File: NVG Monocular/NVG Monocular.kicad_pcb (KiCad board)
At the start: 2 copper layers, 26 parts, among them J1 USB4105-GF-A, J2 breakout to header pin, J3 I2C Breakout, J4 breakout to batt, U1 MP2696AGQ-0000-P

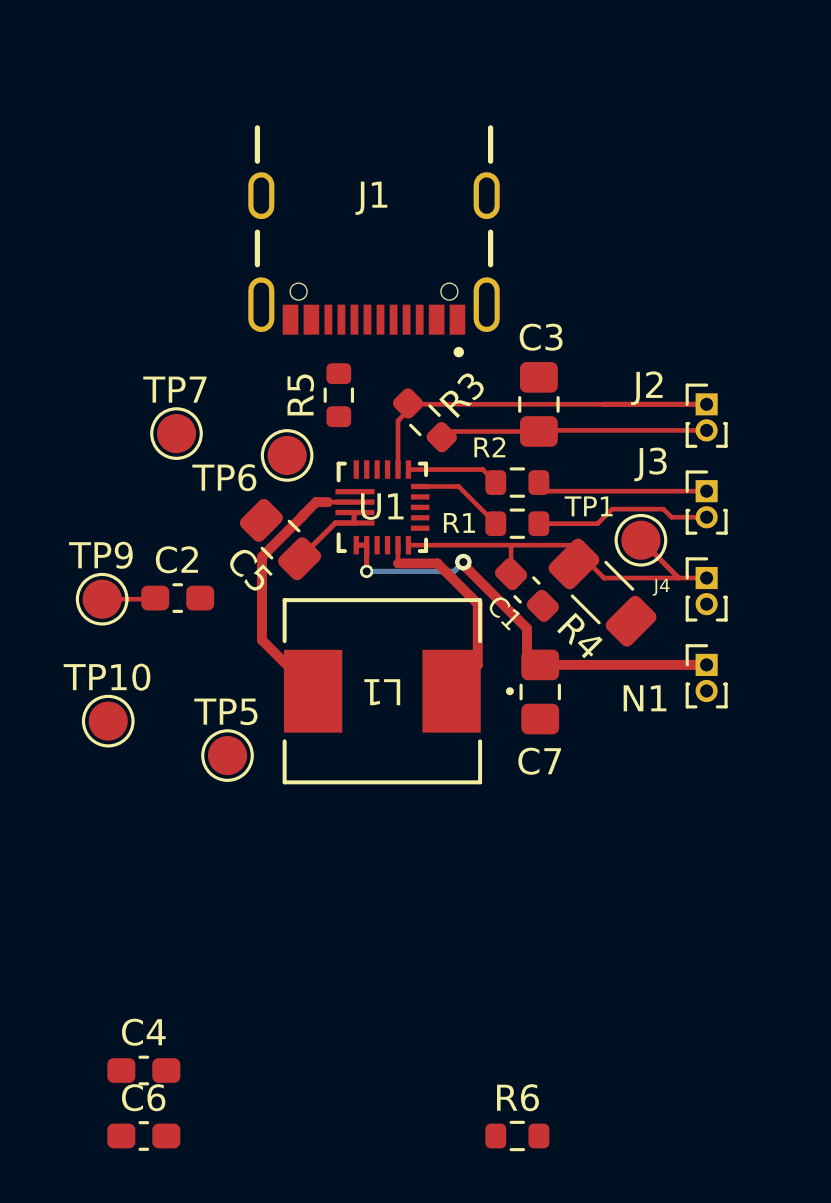
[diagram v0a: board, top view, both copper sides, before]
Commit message: V1 breakout completed and ordered
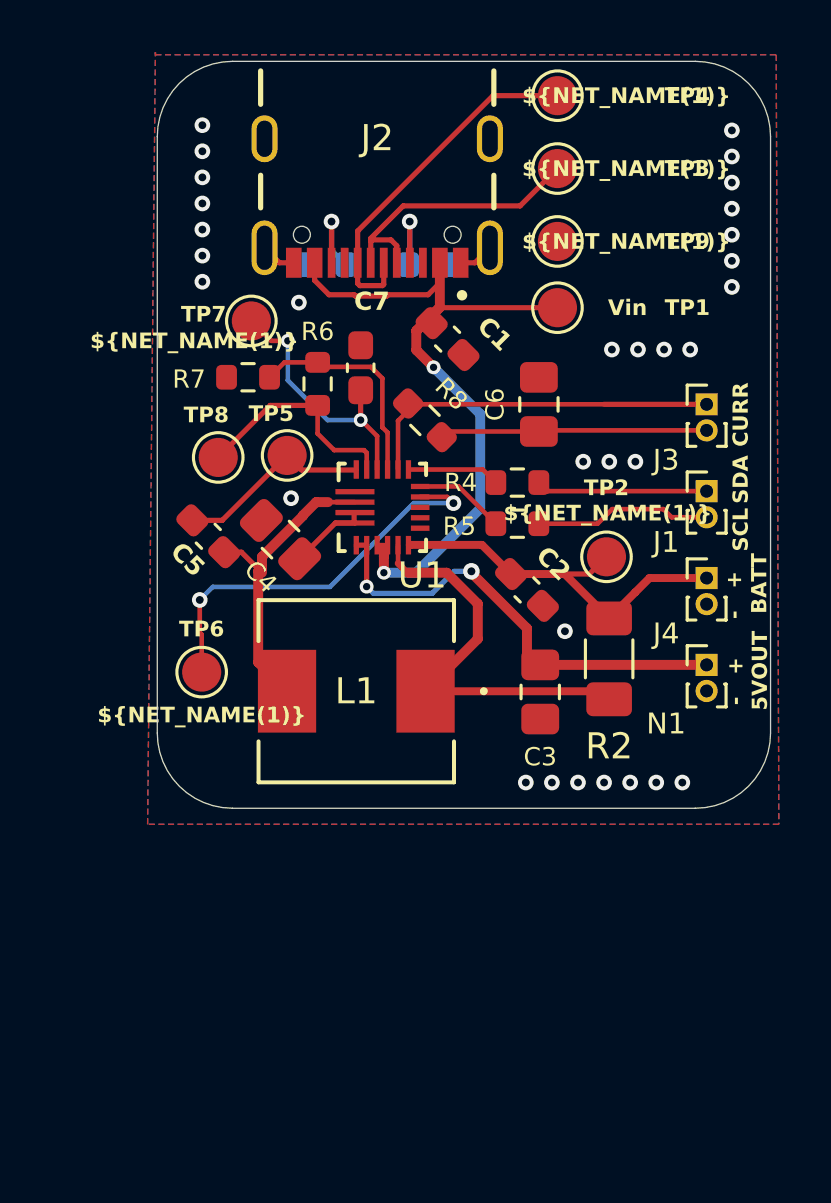
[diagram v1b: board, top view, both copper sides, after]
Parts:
- added G***: LOGO, LOGO, B.Cu at (144.8, 94.9)
- added R1: 10k, Resistor_SMD:R_0603_1608Metric, B.Cu at (148.3, 80.6)
- added R3: 10k, Resistor_SMD:R_0603_1608Metric, B.Cu at (144.3, 80.6)
- added TP1: VBUS, TestPoint:TestPoint_Pad_D1.5mm, F.Cu at (153.2, 82.3)
- added TP3: D-, TestPoint:TestPoint_Pad_D1.5mm, F.Cu at (153.2, 77.0)
- added TP4: D+, TestPoint:TestPoint_Pad_D1.5mm, F.Cu at (153.2, 74.2)
- moved C1 32.7 mm to (149.0, 83.5), turned to -45 degrees
- moved R7 30.9 mm to (141.4, 85.0), turned to 180 degrees
- moved TP9 23.4 mm to (153.2, 79.8)
- moved C5 20.6 mm to (139.8, 91.1), turned to -45 degrees
- moved TP7 12.1 mm to (141.5, 82.8)
- moved C7 11.3 mm to (145.7, 84.6), turned to 90 degrees
- moved TP6 4.04 mm to (139.6, 96.3)
- moved R2 2.55 mm to (155.2, 95.8), turned to -90 degrees
- moved J2 2.18 mm to (146.3, 75.8)
- moved TP8 1.84 mm to (140.2, 88.0)
- moved TP2 1.47 mm to (155.1, 91.8)
- moved L1 1.00 mm to (145.5, 97.0)
- moved R6 0.92 mm to (144.0, 85.2)
- renumbered C6 to C1, C1 to C2, C7 to C3, C5 to C4, C4 to C5, C3 to C6, C2 to C7, J3 to J1, J1 to J2, J2 to J3, R4 to R2, R2 to R4, R1 to R5, R5 to R6, R6 to R7, R3 to R8, TP1 to TP2, TP6 to TP5, TP10 to TP6, TP9 to TP7, TP7 to TP8, TP5 to TP9
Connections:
- J2 pad A5: unconnected-(J1-CC1-PadA5) -> Net-(J2-CC1)
- J2 pad B5: unconnected-(J1-CC2-PadB5) -> Net-(J2-CC2)
- R6 pad 2: GND -> Net-(U1-NTC)
- R7 pad 1: GND -> Net-(U1-NTC)
- U1 pad 18: GND -> Net-(U1-NTC)
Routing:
- net /8_IN: track 0.00 -> 29.9 mm, vias 0 -> 2
- net /INT: track 0.00 -> 15.4 mm, vias 0 -> 2
- net /D+: track 0.00 -> 13.7 mm
- net /D-: track 0.00 -> 11.0 mm
- net Net-(U1-VRNTC): track 0.00 -> 8.54 mm
- net Net-(U1-NTC): track 0.00 -> 8.39 mm
- net /VCC: track 2.05 -> 9.97 mm, vias 0 -> 2
- net Net-(U1-BST): track 0.00 -> 7.55 mm
- net Net-(U1-CSP): track 8.17 -> 14.7 mm
- net Net-(J2-CC2): track 0.00 -> 3.46 mm, vias 0 -> 1
- net Net-(J2-CC1): track 0.00 -> 3.25 mm, vias 0 -> 1
- net GND: track 0.00 -> 2.72 mm, vias 0 -> 31
- net Net-(U1-SW): track 10.4 -> 12.1 mm
- net /6_SYS: track 16.9 -> 17.6 mm
- added copper zone on B.Cu, net GND
- added copper zone on F.Cu, net GND
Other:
- board outline added: 23.5 x 28.6 mm
- board text added: "+"
- board text added: "-"
- board text added: "5VOUT"
- board text added: "BATT"
- board text added: "CURR"
- board text added: "MP2696A Breakout V1 Made with <3 by Siwen Long"
- board text added: "SCL"
- board text added: "SDA"
- board text added: "Vin"
